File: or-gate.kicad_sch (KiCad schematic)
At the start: 6 parts, among them Q1 NPN, Q2 NPN, Q3 NPN

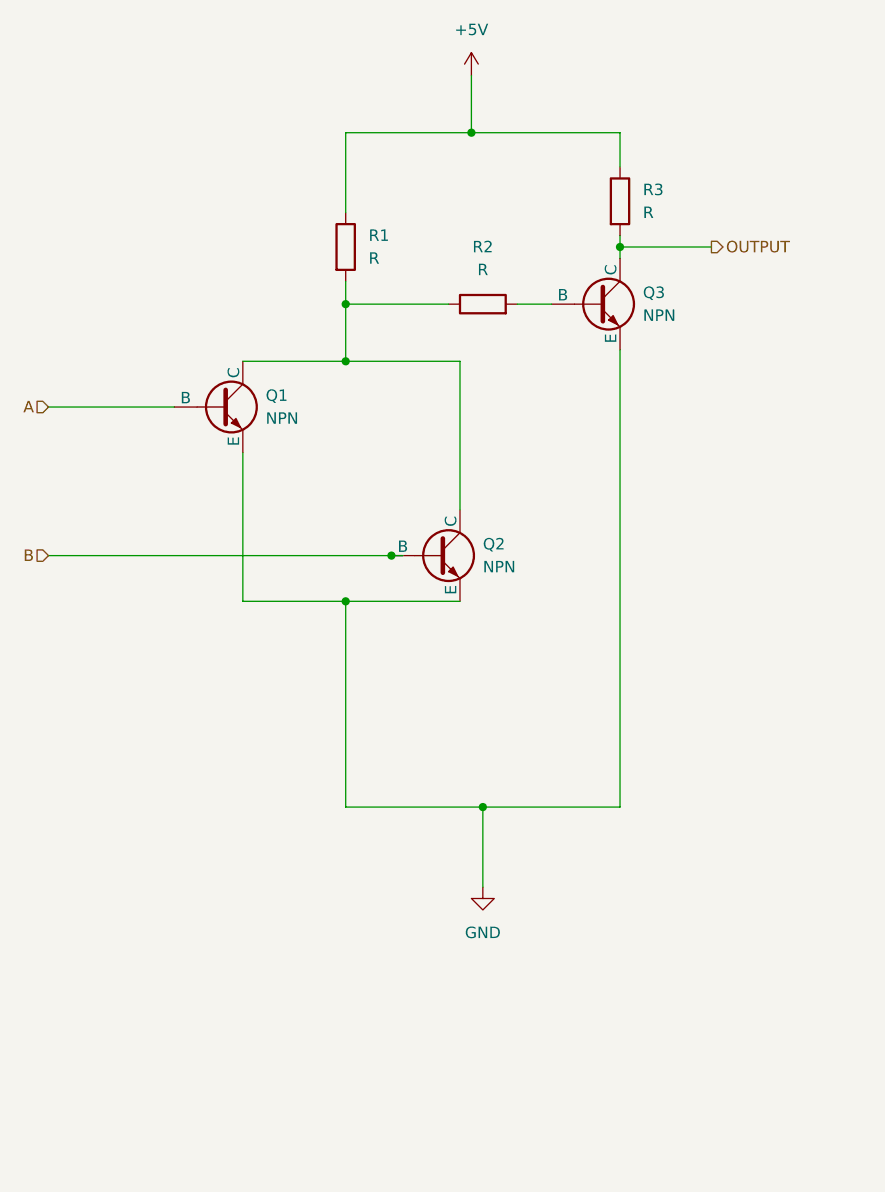
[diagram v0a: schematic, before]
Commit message: Create PCB layout
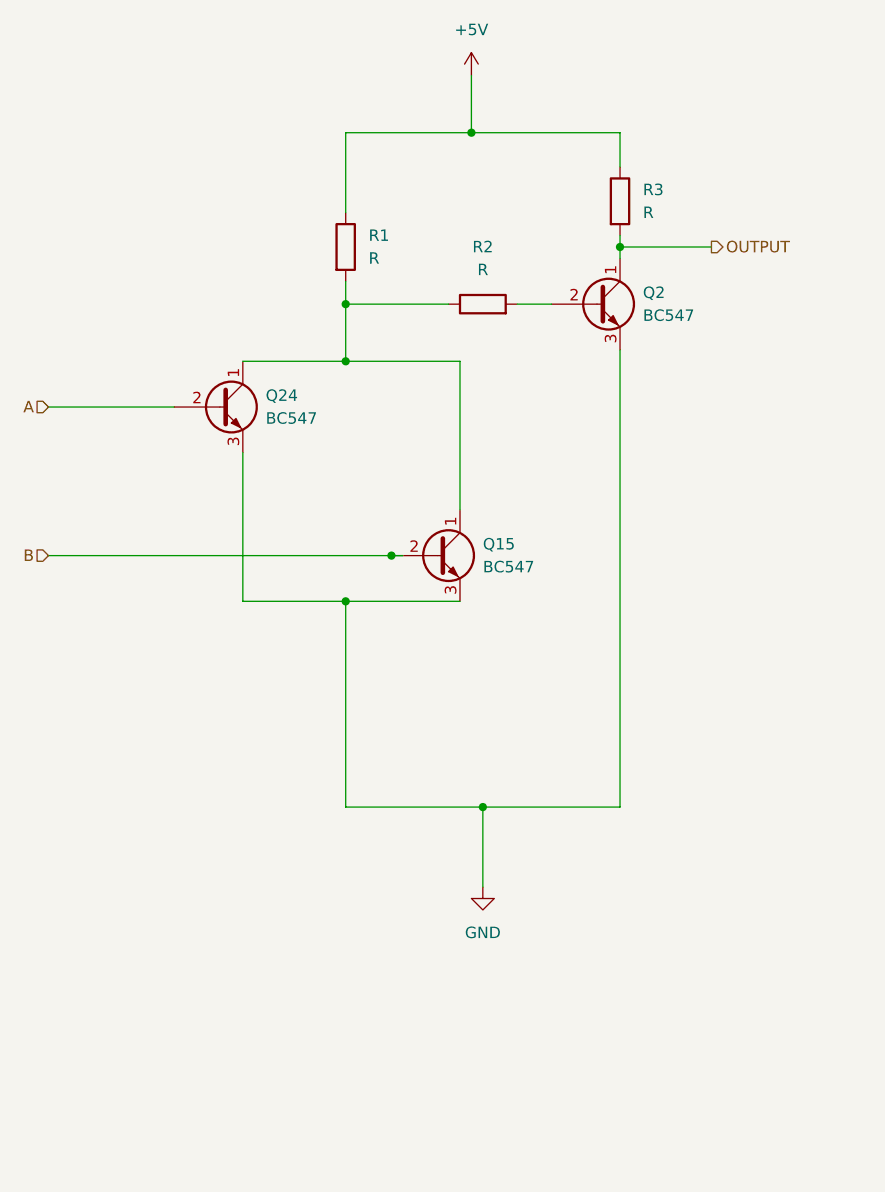
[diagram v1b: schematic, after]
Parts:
- removed Q1, Q2, Q3: NPN, symbol Simulation_SPICE:NPN
- added Q15, Q2, Q24: BC547, Package_TO_SOT_THT:TO-92_Inline, symbol Transistor_BJT:BC547
- R1, R2, R3: footprint (none) -> Resistor_SMD:R_0201_0603Metric
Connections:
- net A: now also Q24.2 (B)
- net B: now also Q15.2 (B)
- net GND: now also Q15.3 (E), Q2.3 (E), Q24.3 (E)
- net OUTPUT: now also Q2.1 (C)
- net at R1.2, R2.1: now also Q15.1 (C), Q24.1 (C)
- net at R2.2: now also Q2.2 (B)

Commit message: Use reusable or gate in half adder
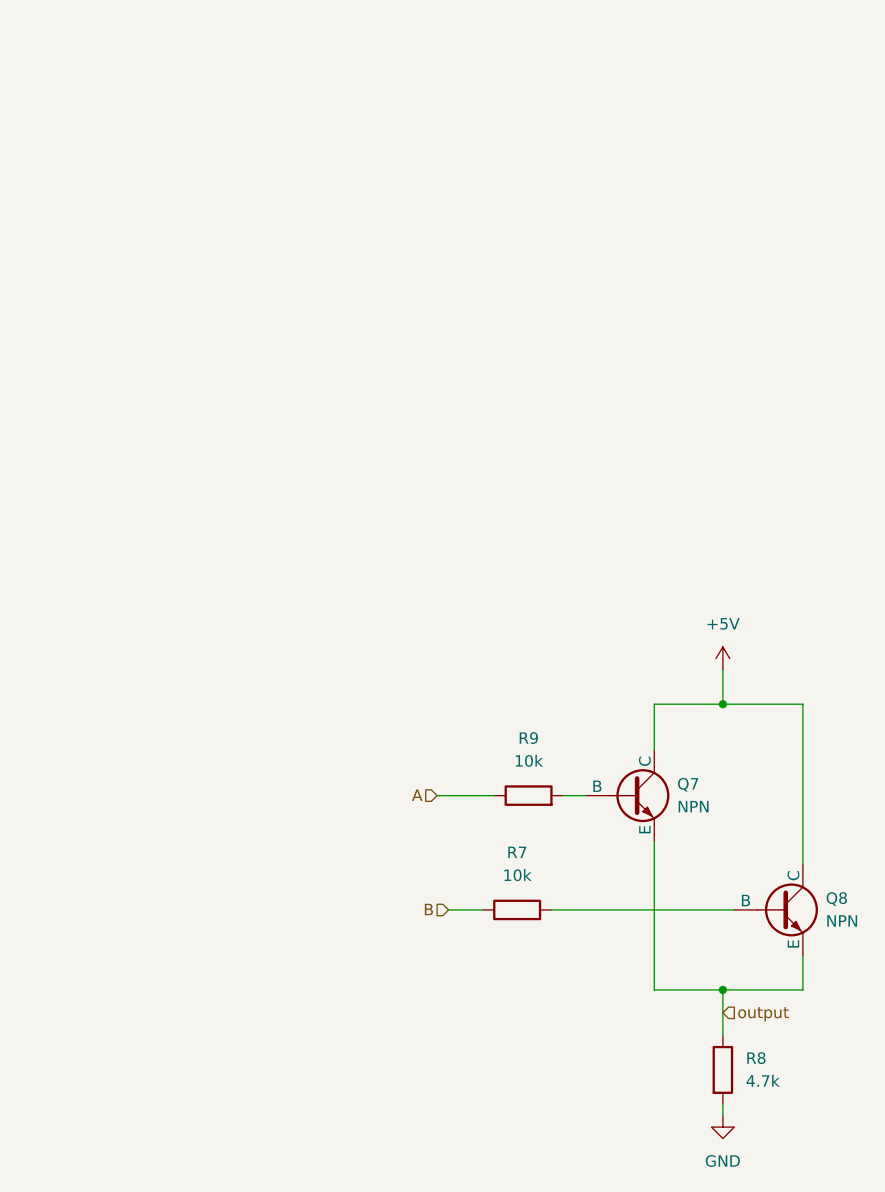
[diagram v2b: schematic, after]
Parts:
- removed Q15, Q2, Q24: BC547, Package_TO_SOT_THT:TO-92_Inline, symbol Transistor_BJT:BC547
- removed R1, R2, R3: R, Resistor_SMD:R_0201_0603Metric, symbol Device:R
- added Q7, Q8: NPN, symbol Simulation_SPICE:NPN
- added R7, R9: 10k, symbol Device:R
- added R8: 4.7k, symbol Device:R
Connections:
- net +5V: now also Q7.1 (C), Q8.1 (C)
- net A: now also R9.1
- net B: now also R7.1
- net GND: now also R8.2
- new net: Q7.2 (B), R9.2
- new net: Q8.2 (B), R7.2
- new net output: Q7.3 (E), Q8.3 (E), R8.1
